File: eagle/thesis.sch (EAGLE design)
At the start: 36 parts, among them Q1 BSS138, Q3 BSS138, U1 ITG-3200, U2 ADXL362, U3 MAX232PTH

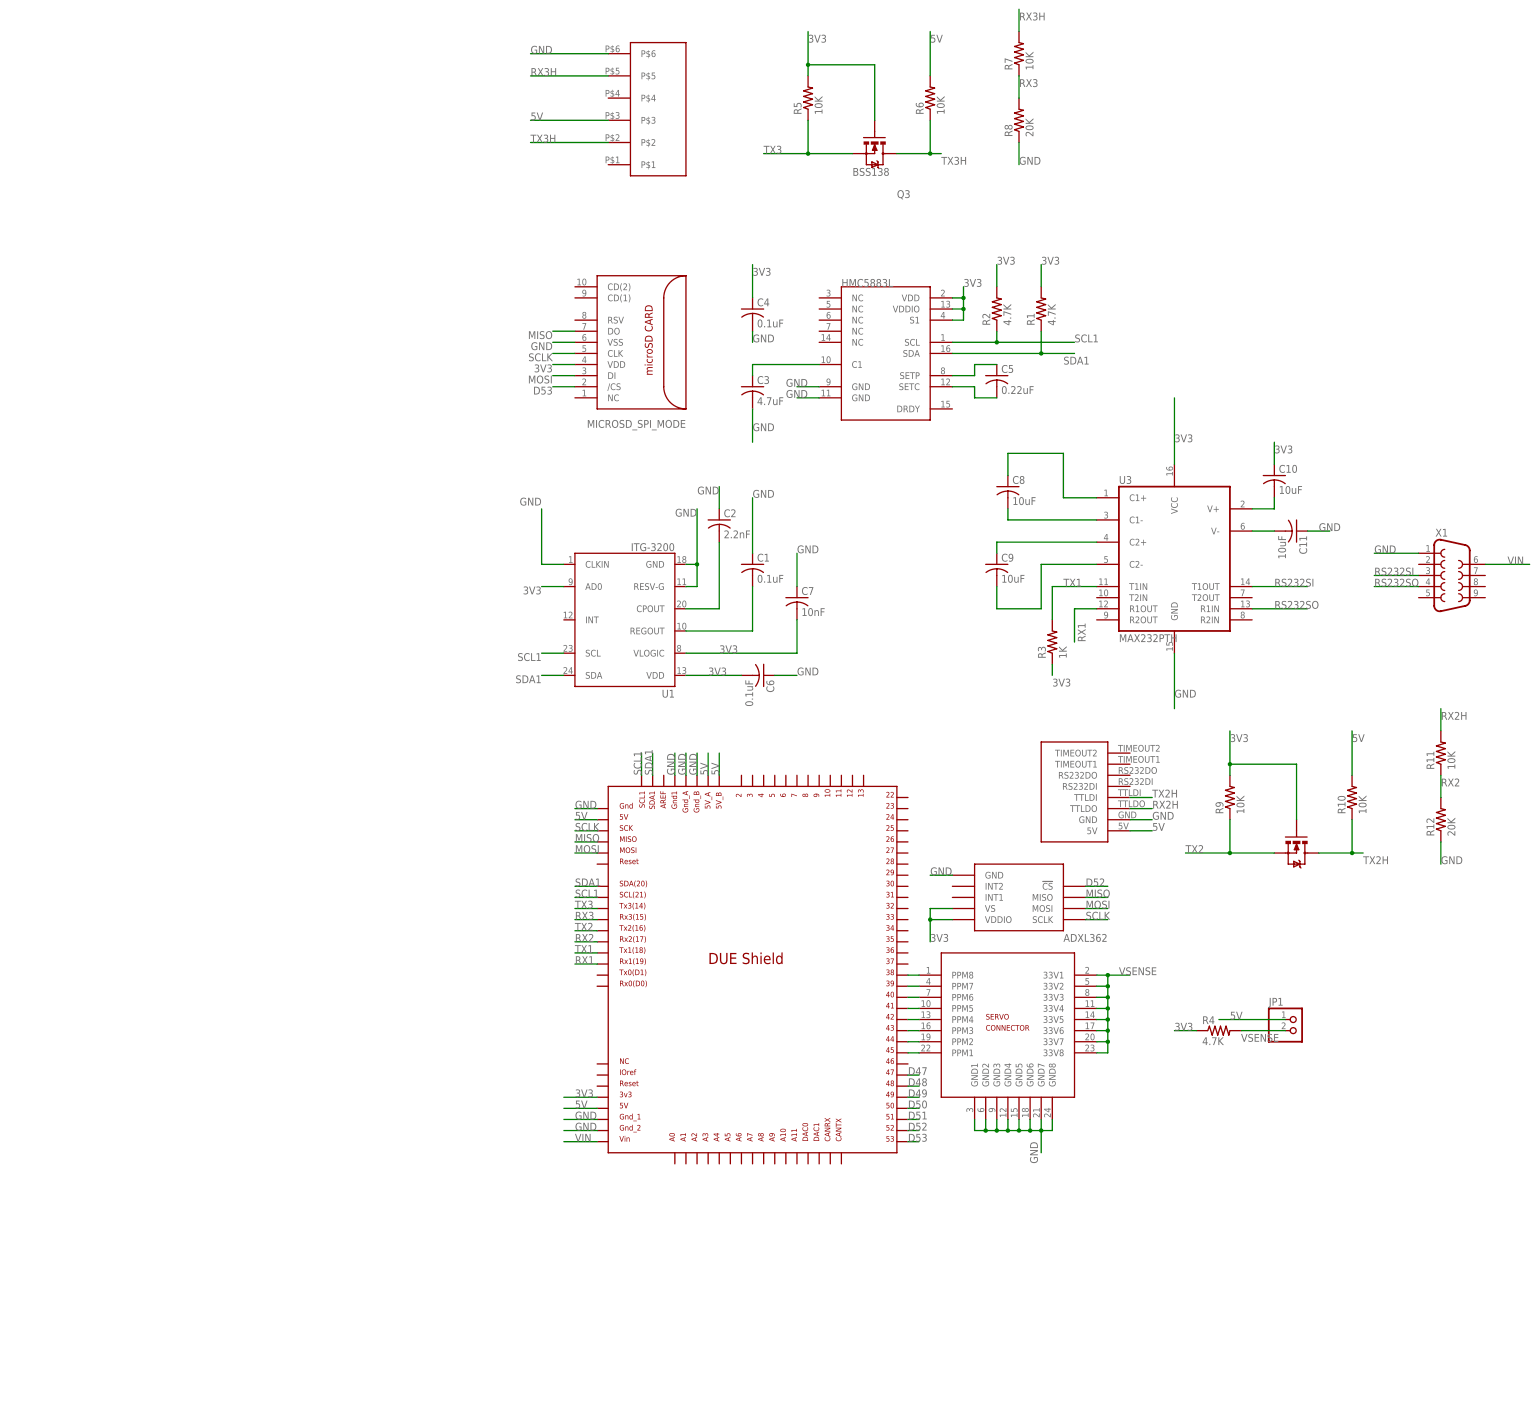
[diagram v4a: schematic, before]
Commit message: modified gps board pad drill size and made thesis board a BOB.
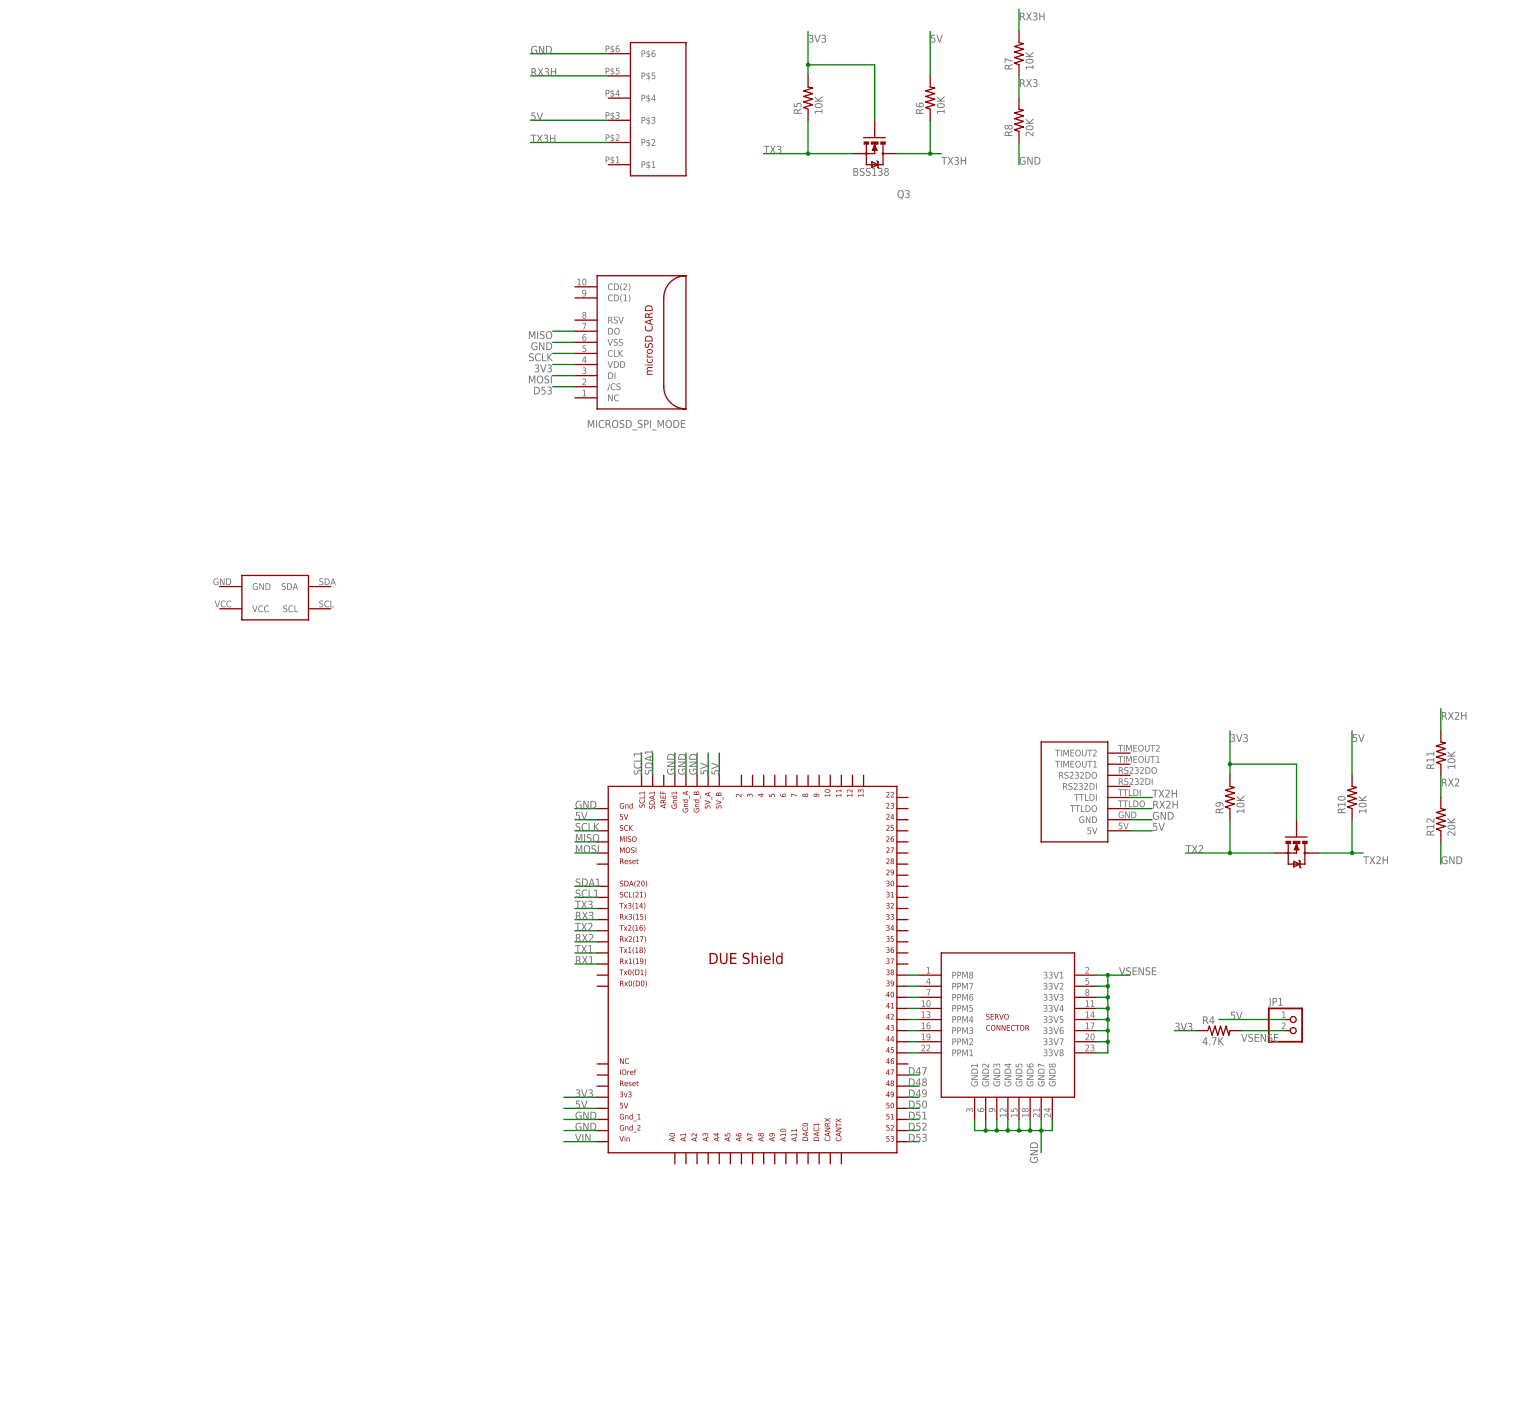
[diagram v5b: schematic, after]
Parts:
- removed C1, C4, C6: 0.1uF, rcl:C-USC0603K
- removed C10, C11, C8, C9: 10uF, rcl:C-USC0603K
- removed C2: 2.2nF, rcl:C-USC0603K
- removed C3: 4.7uF, rcl:C-USC0603K
- removed C5: 0.22uF, rcl:C-USC0603K
- removed C7: 10nF, rcl:C-USC0603K
- removed HMC5883L: SPARKFUN_HMC5883LSMD, HMC5883L_Breakout-v11:SPARKFUN_HMC5883LSMD
- removed R1, R2: 4.7K, rcl:R-US_R0603
- removed R3: 1K, rcl:R-US_R0603
- removed U1: ITG-3200, SparkFun:ITG-3200
- removed U2: ADXL362, SparkFun-Sensors:ADXL362
- removed U3: MAX232PTH, SparkFun-DigitalIC:MAX232PTH
- removed X1: (no value), con-subd:F09VP
- added U$4: HMC5883L, HMC5883L:HMC5883L
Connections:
- removed net CPOUT: C2.2, U1.CPOUT
- removed net N$1: C10.2, U3.V+
- removed net N$12: C3.1, HMC5883L.C1
- removed net N$14: C1.2, U1.REGOUT
- removed net N$2: C11.2, U3.V-
- removed net N$3: C9.1, U3.C2+
- removed net N$4: C9.2, U3.C2-
- removed net N$5: C5.1, HMC5883L.SETP
- removed net N$6: C8.1, U3.C1+
- removed net N$7: C5.2, HMC5883L.SETC
- removed net N$8: C8.2, U3.C1-
- removed net RS232SI: U3.T1OUT, X1.3
- removed net RS232SO: U3.R1IN, X1.4
- net 3V3: no longer C10.1, C4.1, C6.2, C7.2, HMC5883L.S1, HMC5883L.VDD, HMC5883L.VDDIO, R1.2, R2.2, R3.1, U1.AD0, U1.VDD, U1.VLOGIC, U2.VDDIO, U2.VS, U3.VCC
- net D52: no longer U2.!CS
- net GND: no longer C1.1, C11.1, C2.1, C3.2, C4.2, C6.1, C7.1, HMC5883L.GND@1, HMC5883L.GND@2, U1.CLKIN, U1.GND, U1.RESV-G, U2.GND, U3.GND, X1.1
- net MISO: no longer U2.MISO
- net MOSI: no longer U2.MOSI
- net RX1: no longer U3.R1OUT
- net SCL1: no longer HMC5883L.SCL, R2.1, U1.SCL
- net SCLK: no longer U2.SCLK
- net SDA1: no longer HMC5883L.SDA, R1.1, U1.SDA
- net TX1: no longer R3.2, U3.T1IN
- net VIN: no longer X1.6

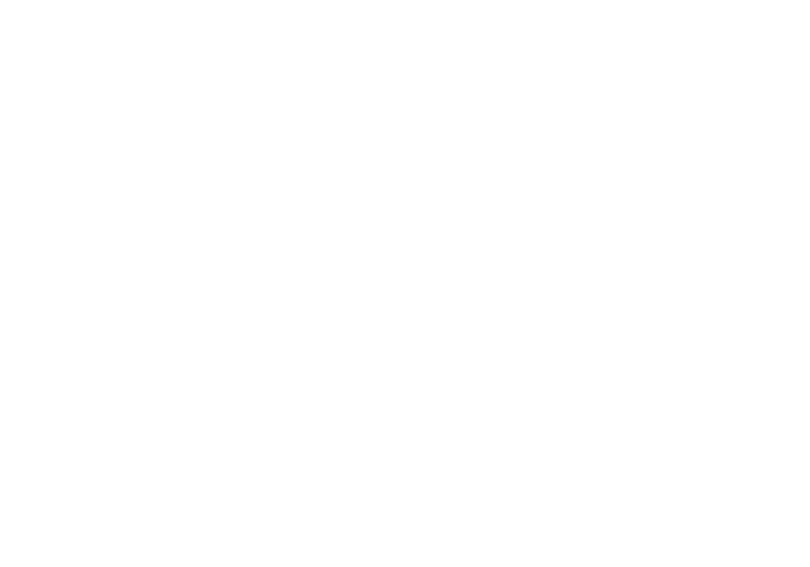
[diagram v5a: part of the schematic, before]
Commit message: added itg3200
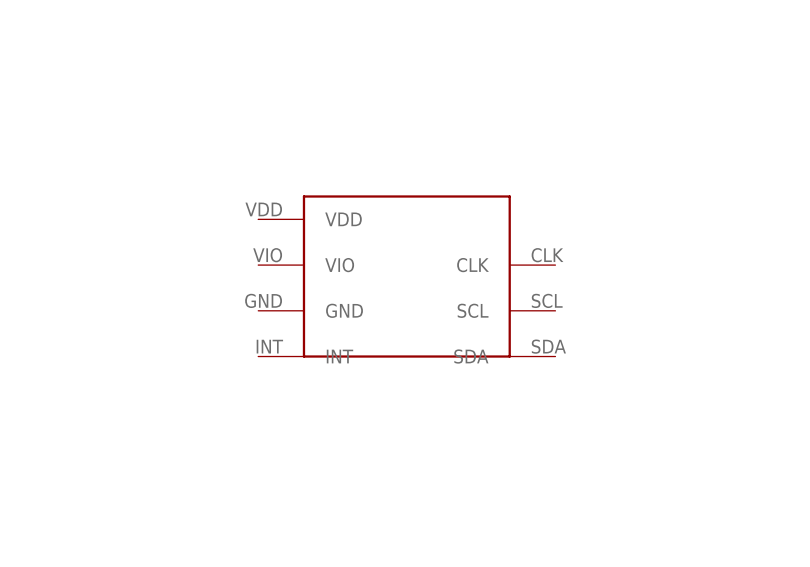
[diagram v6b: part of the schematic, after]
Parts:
- added U$7: ITG3200, ITG3200:ITG3200
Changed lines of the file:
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@@
 <part name="R12" library="rcl" deviceset="R-US_" device="R0603" value="20K"/>
 <part name="U$4" library="HMC5883L" deviceset="HMC5883L" device=""/>
+<part name="U$7" library="ITG3200" deviceset="ITG3200" device=""/>
 </parts>
 <sheets>
@@
 <instance part="R12" gate="G$1" x="190.5" y="76.2" rot="R90"/>
 <instance part="U$4" gate="G$1" x="-83.82" y="121.92"/>
+<instance part="U$7" gate="G$1" x="106.68" y="139.7"/>
 </instances>
 <busses>

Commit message: modified main thesis boards and made changes to the GUI
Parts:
- removed JP1: (no value), pinhead:PINHD-1X2
- removed U$3: RJ11V, RJ11V:RJ11V
- added C1, C2: 0.1uF, rcl:C-USC0603
- added D13, D14, D9: BAT54, diode:BAT54
- added F1, F2, F3: PTCPTH, SparkFun-PowerIC:PTCPTH
- added JP3: (no value), pinhead:PINHD-1X3
- added R1, R13, R3: 10K, rcl:R-US_R0603
- added R14, R2: 20K, rcl:R-US_R0603
- added U$8: ADXL362, adxl362:ADXL362
- added X1: (no value), con-subd:HF15V
- R4: value 4.7K -> 20K
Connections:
- removed net D49: U$1.49
- removed net D50: U$1.50
- removed net D51: U$1.51
- removed net RX3: R7.1, R8.2, U$1.RX3
- removed net RX3H: R7.2, U$3.P$5
- new net 5VNF: F2.1, U$1.5V, U$1.5V_A, U$1.5V_B, U$1.GND_ICSP
- new net ACCEL2CS: X1.4
- new net ACCELCS: U$1.50, U$8.CS
- new net N$10: F3.1, U$1.VIN
- new net N$12: F1.1, U$1.3V3
- new net N$14: X1.14
- new net N$15: X1.15
- new net N$16: D14.C, U$2./CS
- new net N$17: D9.C, U$2.CLK
- new net N$18: D13.C, U$2.DI
- new net N$19: U$7.INT
- new net RX31: R7.1, R8.2, U$1.23
- new net RX32: R1.1, R2.2, U$1.24
- new net RX33: R3.1, R4.2, U$1.25
- new net RX34: R13.1, R14.2, U$1.26
- new net RXH31: R7.2, X1.5
- new net RXH32: R1.2, X1.10
- new net RXH33: R3.2, X1.11
- new net RXH34: R13.2, X1.12
- new net SDCARDCS: D14.A, U$1.51
- new net TEMPBUS: U$1.49, X1.13
- net 3V3: now also C1.1, C2.1, F1.2, JP3.3, U$4.VCC, U$7.VDD, U$7.VIO, U$8.VCC; no longer R4.1, U$1.3V3
- net 5V: now also F2.2, JP3.1, X1.1; no longer JP1.1, U$1.5V, U$1.5V_A, U$1.5V_B, U$1.GND_ICSP, U$3.P$3
- net D53: no longer U$2./CS
- net GND: now also C1.2, C2.2, R14.1, R2.1, R4.1, U$4.GND, U$7.GND, U$8.GND, X1.2; no longer U$3.P$6
- net MISO: now also U$8.MISO, X1.7
- net MOSI: now also D13.A, U$8.MOSI, X1.3; no longer U$2.DI
- net SCL1: now also U$4.SCL, U$7.SCL
- net SCLK: now also D9.A, U$8.SCK, X1.8; no longer U$2.CLK
- net SDA1: now also U$4.SDA, U$7.SDA
- net TX3: now also U$1.22; no longer U$1.TX3
- net TX3H: now also X1.9; no longer U$3.P$2
- net VIN: now also F3.2; no longer U$1.VIN
- net VSENSE: now also JP3.2; no longer JP1.2, R4.2
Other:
- moved on the sheet: R4

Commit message: in middle of writing for AIAA paper
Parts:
- removed R1, R13, R3: 10K, rcl:R-US_R0603
- removed R14, R2, R4: 20K, rcl:R-US_R0603
- added D1: BAT54, diode:BAT54
- renumbered F1 to PTC2, F2 to PTC1, F3 to PTC3
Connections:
- net RXH31 renamed RX3H
- removed net D52: U$1.52
- removed net D53: U$1.53
- removed net N$14: X1.14
- removed net N$15: X1.15
- removed net RX31: R7.1, R8.2, U$1.23
- removed net RX32: R1.1, R2.2, U$1.24
- removed net RX33: R3.1, R4.2, U$1.25
- removed net RX34: R13.1, R14.2, U$1.26
- removed net RXH32: R1.2, X1.10
- removed net RXH33: R3.2, X1.11
- removed net RXH34: R13.2, X1.12
- new net D46: U$1.46, X1.13
- new net RX3: R7.1, R8.2, U$1.RX3
- new net SDDETECT: U$1.52, U$2.CD(1)
- new net VSENSED: D1.C, U$5.33V1, U$5.33V2, U$5.33V3, U$5.33V4, U$5.33V5, U$5.33V6, U$5.33V7, U$5.33V8
- net D47: now also X1.14
- net D48: now also X1.15
- net GND: no longer R14.1, R2.1, R4.1
- net SCL1: now also X1.12
- net SDA1: now also X1.11
- net TEMPBUS: now also X1.10; no longer X1.13
- net TX3: now also U$1.TX3; no longer U$1.22
- net VSENSE: now also D1.A; no longer U$5.33V1, U$5.33V2, U$5.33V3, U$5.33V4, U$5.33V5, U$5.33V6, U$5.33V7, U$5.33V8
